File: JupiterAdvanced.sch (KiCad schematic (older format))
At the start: 220 parts

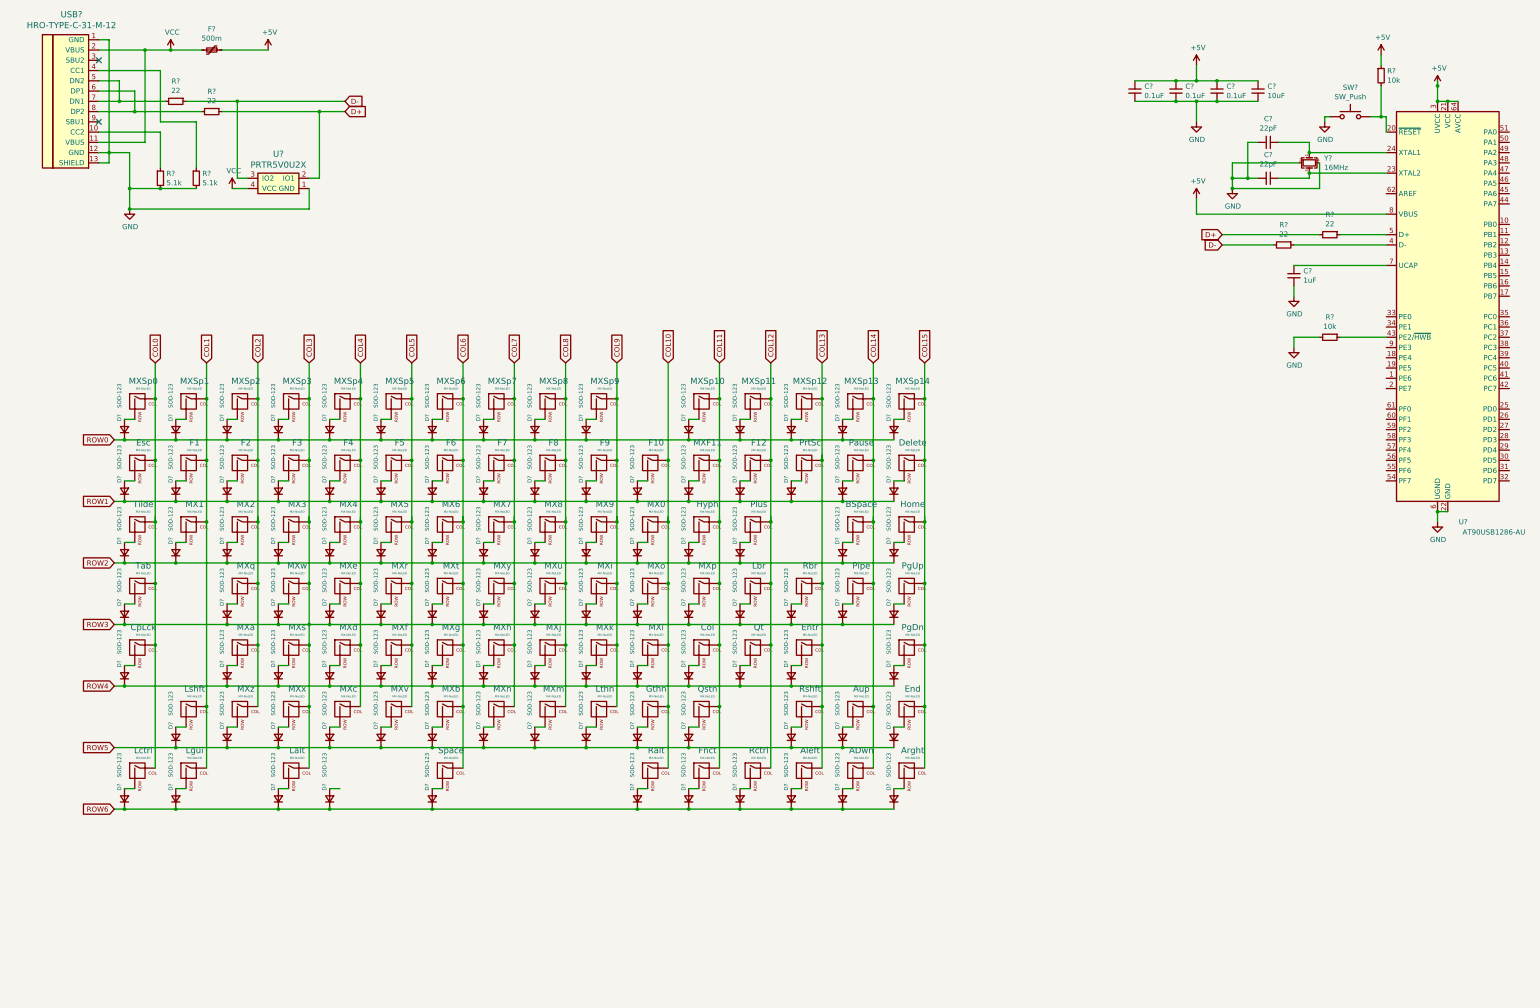
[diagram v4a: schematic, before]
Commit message: All footprints added
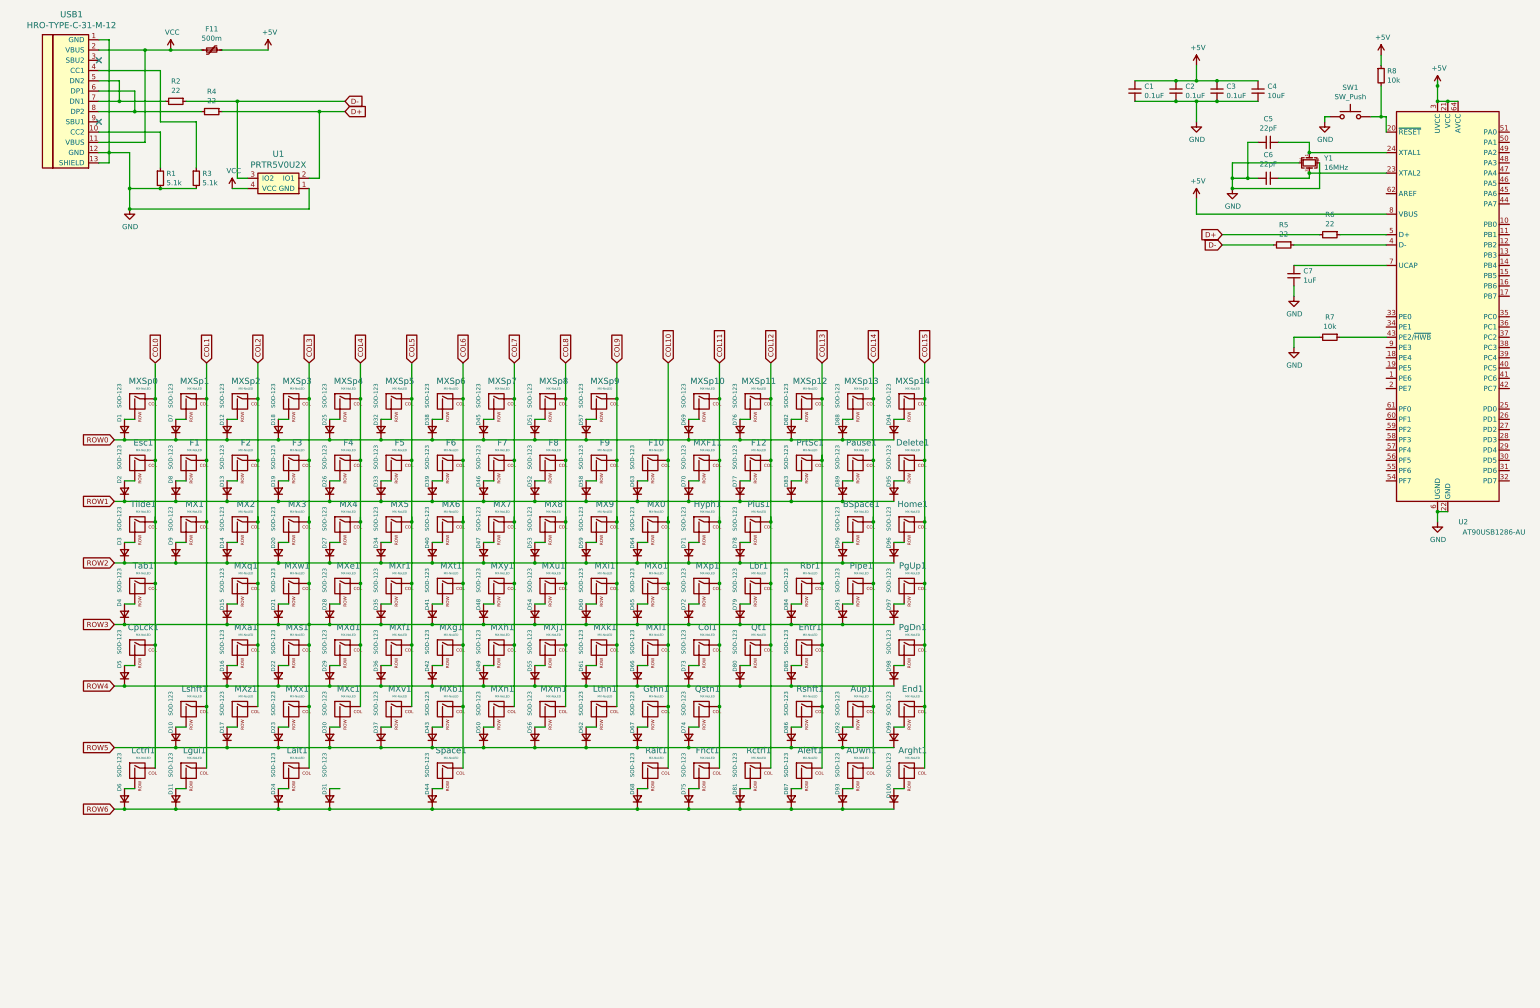
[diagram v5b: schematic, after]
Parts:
- ADwn1: renamed from ADwn; footprint (none) -> MX_Only:MXOnly-1U-NoLED
- Aleft1: renamed from Aleft; footprint (none) -> MX_Only:MXOnly-1U-NoLED
- Arght1: renamed from Arght; footprint (none) -> MX_Only:MXOnly-1U-NoLED
- Aup1: renamed from Aup; footprint (none) -> MX_Only:MXOnly-1U-NoLED
- BSpace1: renamed from BSpace; footprint (none) -> MX_Only:MXOnly-2U-NoLED
- C1, C2, C3, C4, C5, C6, C7: renamed from C?; footprint (none) -> Capacitor_SMD:C_0805_2012Metric
- Col1: renamed from Col; footprint (none) -> MX_Only:MXOnly-1U-NoLED
- CpLck1: renamed from CpLck; footprint (none) -> MX_Only:MXOnly-1.75U-NoLED
- D1, D10, D100, D11, D12, D13, D14, D15, D16, D17, D18, D19, D2, D20, D21, D22, D23, D24, D25, D26, D27, D28, D29, D3, D30, D31, D32, D33, D34, D35, D36, D37, D38, D39, D4, D40, D41, D42, D43, D44, D45, D46, D47, D48, D49, D5, D50, D51, D52, D53, D54, D55, D56, D57, D58, D59, D6, D60, D61, D62, D63, D64, D65, D66, D67, D68, D69, D7, D70, D71, D72, D73, D74, D75, D76, D77, D78, D79, D8, D80, D81, D82, D83, D84, D85, D86, D87, D88, D89, D9, D90, D91, D92, D93, D94, D95, D96, D97, D98, D99: renamed from D?; footprint (none) -> Diode_SMD:D_SOD-123
- Delete1: renamed from Delete; footprint (none) -> MX_Only:MXOnly-1U-NoLED
- End1: renamed from End; footprint (none) -> MX_Only:MXOnly-1U-NoLED
- Entr1: renamed from Entr; footprint (none) -> MX_Only:MXOnly-2.25U-NoLED
- Esc1: renamed from Esc; footprint (none) -> MX_Only:MXOnly-1U-NoLED
- F1, F10, F12, F2, F3, F4, F5, F6, F7, F8, F9, MX0, MX1, MX2, MX3, MX4, MX5, MX6, MX7, MX8, MX9, MXF11, MXSp0, MXSp1, MXSp10, MXSp11, MXSp12, MXSp13, MXSp14, MXSp2, MXSp3, MXSp4, MXSp5, MXSp6, MXSp7, MXSp8, MXSp9: footprint (none) -> MX_Only:MXOnly-1U-NoLED
- F11: renamed from F?; footprint (none) -> Fuse:Fuse_1206_3216Metric
- Fnct1: renamed from Fnct; footprint (none) -> MX_Only:MXOnly-1U-NoLED
- Gthn1: renamed from Gthn; footprint (none) -> MX_Only:MXOnly-1U-NoLED
- Home1: renamed from Home; footprint (none) -> MX_Only:MXOnly-1U-NoLED
- Hyph1: renamed from Hyph; footprint (none) -> MX_Only:MXOnly-1U-NoLED
- Lalt1: renamed from Lalt; footprint (none) -> MX_Only:MXOnly-1.25U-NoLED
- Lbr1: renamed from Lbr; footprint (none) -> MX_Only:MXOnly-1U-NoLED
- Lctrl1: renamed from Lctrl; footprint (none) -> MX_Only:MXOnly-1.25U-NoLED
- Lgui1: renamed from Lgui; footprint (none) -> MX_Only:MXOnly-1.25U-NoLED
- Lshft1: renamed from Lshft; footprint (none) -> MX_Only:MXOnly-2.25U-NoLED
- Lthn1: renamed from Lthn; footprint (none) -> MX_Only:MXOnly-1U-NoLED
- MXa1: renamed from MXa; footprint (none) -> MX_Only:MXOnly-1U-NoLED
- MXb1: renamed from MXb; footprint (none) -> MX_Only:MXOnly-1U-NoLED
- MXc1: renamed from MXc; footprint (none) -> MX_Only:MXOnly-1U-NoLED
- MXd1: renamed from MXd; footprint (none) -> MX_Only:MXOnly-1U-NoLED
- MXe1: renamed from MXe; footprint (none) -> MX_Only:MXOnly-1U-NoLED
- MXf1: renamed from MXf; footprint (none) -> MX_Only:MXOnly-1U-NoLED
- MXg1: renamed from MXg; footprint (none) -> MX_Only:MXOnly-1U-NoLED
- MXh1: renamed from MXh; footprint (none) -> MX_Only:MXOnly-1U-NoLED
- MXi1: renamed from MXi; footprint (none) -> MX_Only:MXOnly-1U-NoLED
- MXj1: renamed from MXj; footprint (none) -> MX_Only:MXOnly-1U-NoLED
- MXk1: renamed from MXk; footprint (none) -> MX_Only:MXOnly-1U-NoLED
- MXl1: renamed from MXl; footprint (none) -> MX_Only:MXOnly-1U-NoLED
- MXm1: renamed from MXm; footprint (none) -> MX_Only:MXOnly-1U-NoLED
- MXn1: renamed from MXn; footprint (none) -> MX_Only:MXOnly-1U-NoLED
- MXo1: renamed from MXo; footprint (none) -> MX_Only:MXOnly-1U-NoLED
- MXp1: renamed from MXp; footprint (none) -> MX_Only:MXOnly-1U-NoLED
- MXq1: renamed from MXq; footprint (none) -> MX_Only:MXOnly-1U-NoLED
- MXr1: renamed from MXr; footprint (none) -> MX_Only:MXOnly-1U-NoLED
- MXs1: renamed from MXs; footprint (none) -> MX_Only:MXOnly-1U-NoLED
- MXt1: renamed from MXt; footprint (none) -> MX_Only:MXOnly-1U-NoLED
- MXu1: renamed from MXu; footprint (none) -> MX_Only:MXOnly-1U-NoLED
- MXv1: renamed from MXv; footprint (none) -> MX_Only:MXOnly-1U-NoLED
- MXw1: renamed from MXw; footprint (none) -> MX_Only:MXOnly-1U-NoLED
- MXx1: renamed from MXx; footprint (none) -> MX_Only:MXOnly-1U-NoLED
- MXy1: renamed from MXy; footprint (none) -> MX_Only:MXOnly-1U-NoLED
- MXz1: renamed from MXz; footprint (none) -> MX_Only:MXOnly-1U-NoLED
- Pause1: renamed from Pause; footprint (none) -> MX_Only:MXOnly-1U-NoLED
- PgDn1: renamed from PgDn; footprint (none) -> MX_Only:MXOnly-1U-NoLED
- PgUp1: renamed from PgUp; footprint (none) -> MX_Only:MXOnly-1U-NoLED
- Pipe1: renamed from Pipe; footprint (none) -> MX_Only:MXOnly-1U-NoLED
- Plus1: renamed from Plus; footprint (none) -> MX_Only:MXOnly-1U-NoLED
- PrtSc1: renamed from PrtSc; footprint (none) -> MX_Only:MXOnly-1U-NoLED
- Qstn1: renamed from Qstn; footprint (none) -> MX_Only:MXOnly-1U-NoLED
- Qt1: renamed from Qt; footprint (none) -> MX_Only:MXOnly-1U-NoLED
- R1, R2, R3, R4, R5, R6, R7, R8: renamed from R?; footprint (none) -> Resistor_SMD:R_0805_2012Metric
- Ralt1: renamed from Ralt; footprint (none) -> MX_Only:MXOnly-1U-NoLED
- Rbr1: renamed from Rbr; footprint (none) -> MX_Only:MXOnly-1U-NoLED
- Rctrl1: renamed from Rctrl; footprint (none) -> MX_Only:MXOnly-1U-NoLED
- Rshft1: renamed from Rshft; footprint (none) -> MX_Only:MXOnly-1.75U-NoLED
- SW1: renamed from SW?; footprint (none) -> random-keyboard-parts:SKQG-1155865
- Space1: renamed from Space; footprint (none) -> MX_Only:MXOnly-6.25U-NoLED
- Tab1: renamed from Tab; footprint (none) -> MX_Only:MXOnly-1.5U-NoLED
- Tilde1: renamed from Tilde; footprint (none) -> MX_Only:MXOnly-1U-NoLED
- U1: renamed from U?; footprint (none) -> random-keyboard-parts:SOT143B
- USB1: renamed from USB?; footprint (none) -> random-keyboard-parts:Molex-0548190589
- Y1: renamed from Y?; footprint (none) -> Crystal:Crystal_SMD_3225-4Pin_3.2x2.5mm
- gave numbers to parts that had none: 1

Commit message: PCB Switch locations complete
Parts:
- USB1: footprint random-keyboard-parts:Molex-0548190589 -> Type-C:HRO-TYPE-C-31-M-12-Assembly
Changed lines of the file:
@@
 F 0 "USB1" H 1183 2347 60  0000 C CNN
 F 1 "HRO-TYPE-C-31-M-12" H 1183 2241 60  0000 C CNN
-F 2 "random-keyboard-parts:Molex-0548190589" H 1350 1550 60  0001 C CNN
+F 2 "Type-C:HRO-TYPE-C-31-M-12-Assembly" H 1350 1550 60  0001 C CNN
 F 3 "" H 1350 1550 60  0001 C CNN
 	1    1350 1550

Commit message: All diodes placed on PCB (no routes)
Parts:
- removed D31: SOD-123, Diode_SMD:D_SOD-123, symbol Device:D_Small
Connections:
- wire segments 406 -> 404
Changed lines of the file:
@@
 	3300 8300 3200 8300
-$Comp
-L Device:D_Small D31
-U 1 1 61C7F39B
-P 3700 8400
-F 0 "D31" H 3850 8450 39  0000 R CNN
-F 1 "SOD-123" H 4150 8450 39  0000 R CNN
-F 2 "Diode_SMD:D_SOD-123" V 3700 8400 50  0001 C CNN
-F 3 "~" V 3700 8400 50  0001 C CNN
-	1    3700 8400
-	0    -1   -1   0
-$EndComp
-Wire Wire Line
-	3800 8300 3700 8300
 $Comp
 L MX_Alps_Hybrid:MX-NoLED Space1
@@
 	2200 8500 1700 8500
 Connection ~ 3200 8500
-Connection ~ 3700 8500
-Wire Wire Line
-	3700 8500 3200 8500
 Connection ~ 4700 8500
 Connection ~ 6700 8500
@@
 	2200 8500 3200 8500
 Wire Wire Line
-	3700 8500 4700 8500
-Wire Wire Line
 	4700 8500 6700 8500
 Wire Wire Line
@@
 	9500 7500 9500 8100
 Connection ~ 9500 7500
+Wire Wire Line
+	3200 8500 4700 8500
 $EndSCHEMATC

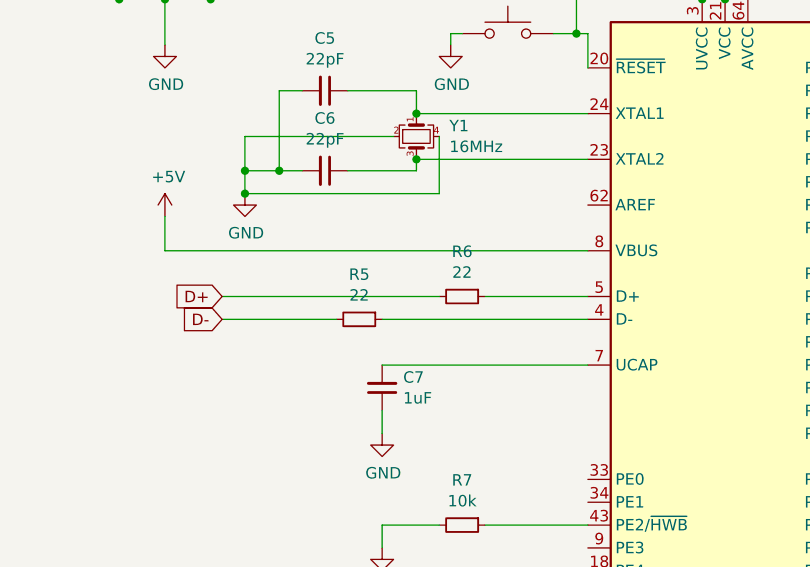
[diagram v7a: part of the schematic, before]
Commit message: Cleaned up USB C connector resistors
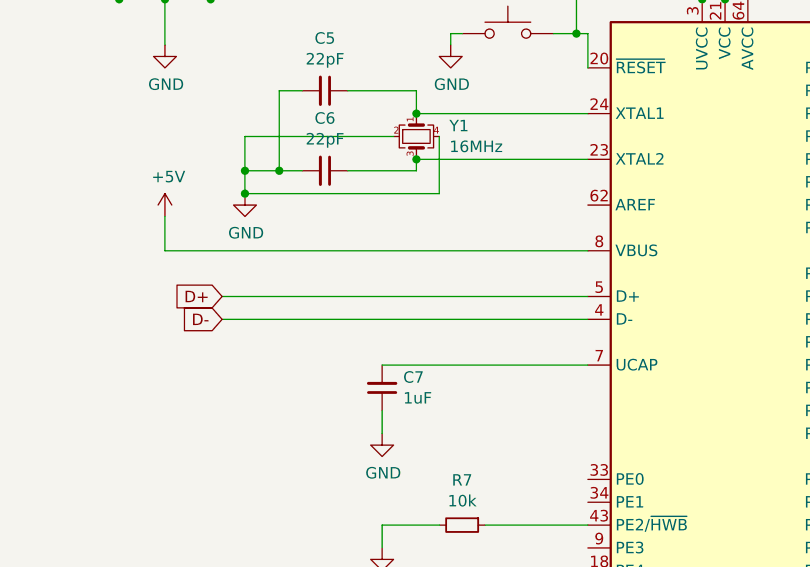
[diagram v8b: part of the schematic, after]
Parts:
- removed R5, R6: 22, Resistor_SMD:R_0805_2012Metric, symbol Device:R_Small
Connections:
- wire segments 404 -> 402
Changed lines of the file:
@@
 	13100 3900 13350 3900
 $Comp
-L Device:R_Small R6
-U 1 1 6073C03D
-P 13450 2900
-F 0 "R6" V 13254 2900 50  0000 C CNN
-F 1 "22" V 13345 2900 50  0000 C CNN
-F 2 "Resistor_SMD:R_0805_2012Metric" H 13450 2900 50  0001 C CNN
-F 3 "~" H 13450 2900 50  0001 C CNN
-	1    13450 2900
-	0    1    1    0
-$EndComp
-$Comp
-L Device:R_Small R5
-U 1 1 6073D3AE
-P 13000 3000
-F 0 "R5" V 12804 3000 50  0000 C CNN
-F 1 "22" V 12895 3000 50  0000 C CNN
-F 2 "Resistor_SMD:R_0805_2012Metric" H 13000 3000 50  0001 C CNN
-F 3 "~" H 13000 3000 50  0001 C CNN
-	1    13000 3000
-	0    1    1    0
-$EndComp
-Wire Wire Line
-	14000 2900 13550 2900
-Wire Wire Line
-	14000 3000 13100 3000
-$Comp
 L Device:C_Small C7
 U 1 1 6073ED4F
@@
 Text GLabel 12400 3000 0    50   Input ~ 0
 D-
-Wire Wire Line
-	12400 3000 12900 3000
-Wire Wire Line
-	12400 2900 13350 2900
 $Comp
 L Type-C:HRO-TYPE-C-31-M-12 USB1
@@
 Wire Wire Line
 	3200 8500 4700 8500
+Wire Wire Line
+	12400 3000 14000 3000
+Wire Wire Line
+	12400 2900 14000 2900
 $EndSCHEMATC
